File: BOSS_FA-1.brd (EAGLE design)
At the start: 50.5 x 41.9 mm, 42 parts, among them IC1 JRC4558, Q1 J201, SW1 SPST

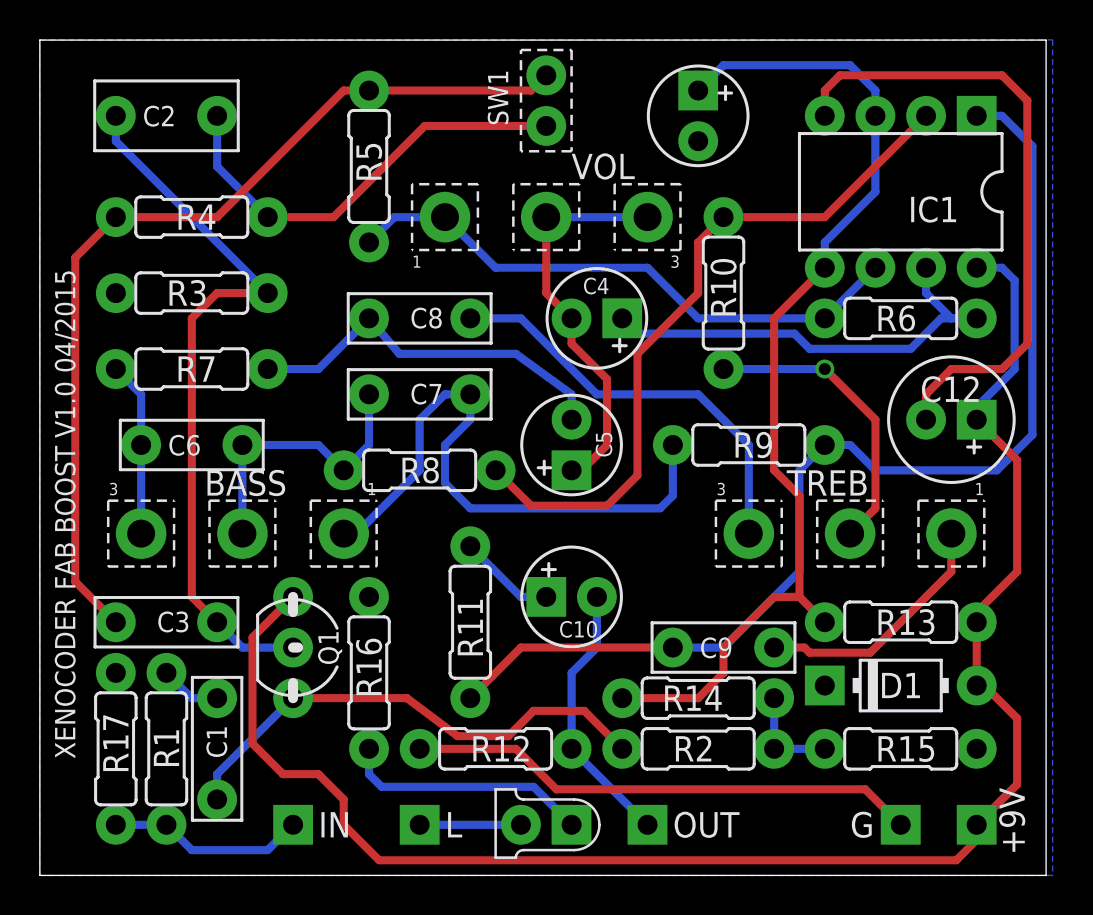
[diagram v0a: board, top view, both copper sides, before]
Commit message: Fixed Diode 1 orientation and connected power rail to LED (Version 1.1)
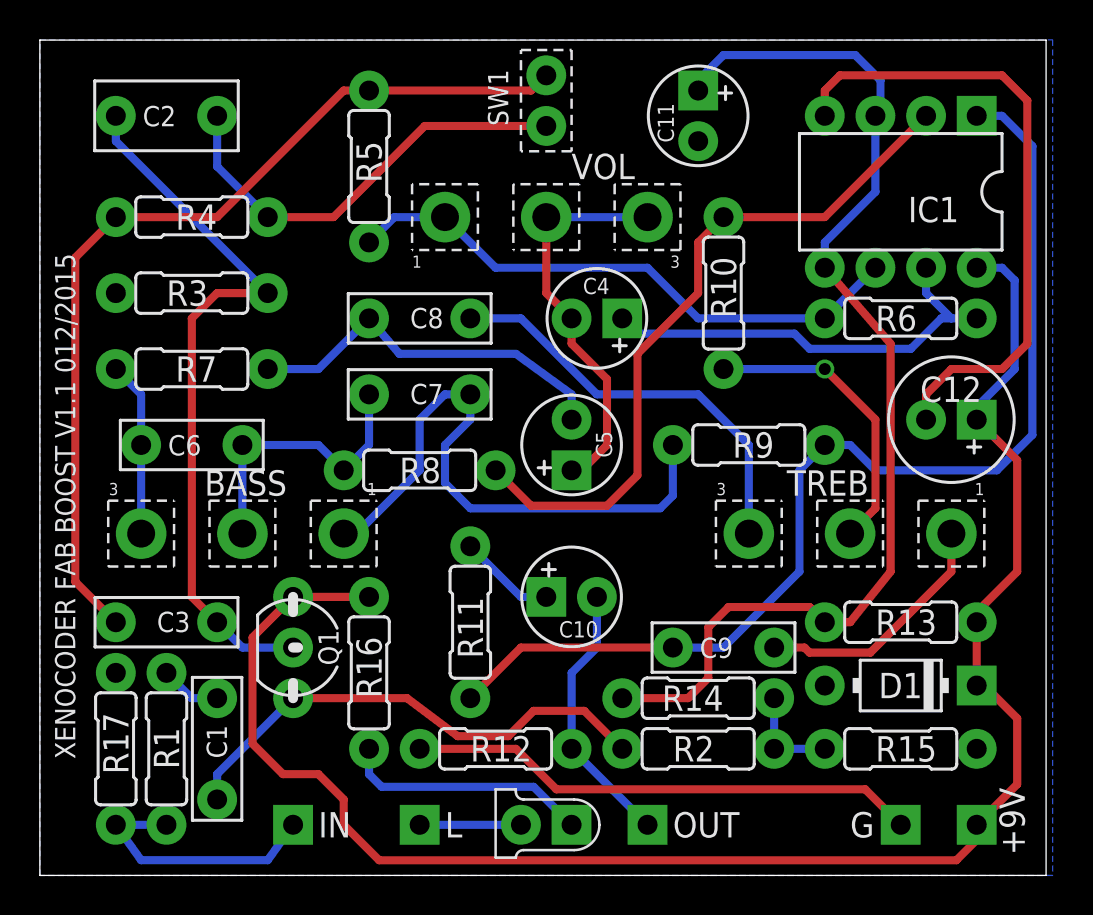
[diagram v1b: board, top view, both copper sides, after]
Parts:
- turned D1 to 180 degrees
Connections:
- net ICNET renamed A
- net LED renamed IN
- net +9V: now also D1.C; no longer D1.A
- net GND: now also D1.A; no longer D1.C
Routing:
- net A: track 51.5 -> 56.1 mm
- net +9V: track 82.7 -> 86.5 mm
- net IN: track 9.94 -> 13.3 mm
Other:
- board text added: "XENOCODER FAB BOOST V1.1 012/2015"
- board text removed: "XENOCODER FAB BOOST V1.0 04/2015"
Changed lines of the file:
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@@
 <?xml version="1.0" encoding="utf-8"?>
 <!DOCTYPE eagle SYSTEM "eagle.dtd">
-<eagle version="7.2.0">
+<eagle version="7.4.0">
 <drawing>
 <settings>
@@
 <wire x1="50.47" y1="41.9" x2="0" y2="41.9" width="0" layer="20"/>
 <wire x1="0" y1="41.9" x2="0" y2="0" width="0" layer="20"/>
-<text x="1.778" y="5.842" size="1.016" layer="25" font="vector" ratio="5" rot="R90">XENOCODER FAB BOOST V1.0 04/2015</text>
+<text x="1.778" y="5.842" size="1.016" layer="25" font="vector" ratio="5" rot="R90">XENOCODER FAB BOOST V1.1 012/2015</text>
 </plain>
 <attributes>
@@
 <attribute name="NAME" x="26.035" y="11.938" size="0.8128" layer="25" ratio="12"/>
 </element>
-<element name="C11" library="mb_caps-electro" package="050_020_1" value="10uF" x="33.02" y="38.1" smashed="yes" rot="R270"/>
+<element name="C11" library="mb_caps-electro" package="050_020_1" value="10uF" x="33.02" y="38.1" smashed="yes" rot="R270">
+<attribute name="NAME" x="30.988" y="38.735" size="0.8128" layer="25" ratio="12" rot="R270"/>
+</element>
 <element name="C12" library="mb_caps-electro" package="063_025" value="100uF" x="45.72" y="22.86" smashed="yes" rot="R180">
 <attribute name="NAME" x="47.244" y="25.019" size="1.27" layer="25" ratio="12" rot="R180"/>
@@
 <attribute name="NAME" x="13.97" y="12.319" size="1.016" layer="25" ratio="12" rot="R270"/>
 </element>
-<element name="D1" library="mb_diodes" package="DO41-3" value="1N4001" x="43.18" y="9.525" smashed="yes">
-<attribute name="NAME" x="42.0878" y="8.89" size="1.27" layer="25" ratio="12"/>
+<element name="D1" library="mb_diodes" package="DO41-3" value="1N4001" x="43.18" y="9.525" smashed="yes" rot="R180">
+<attribute name="NAME" x="44.2722" y="10.16" size="1.27" layer="25" ratio="12" rot="R180"/>
 </element>
 <element name="VOL" library="mb_pots" package="16MM_PCB_PADS" value="A1M" x="25.4" y="33.02" smashed="yes" rot="R180">
@@
 </elements>
 <signals>
-<signal name="LED">
-<contactref element="IN" pad="1"/>
-<contactref element="R17" pad="1"/>
-<contactref element="R1" pad="1"/>
-<wire x1="12.7" y1="2.54" x2="11.43" y2="1.27" width="0.4064" layer="16"/>
-<wire x1="11.43" y1="1.27" x2="7.62" y2="1.27" width="0.4064" layer="16"/>
-<wire x1="7.62" y1="1.27" x2="6.35" y2="2.54" width="0.4064" layer="16"/>
-<wire x1="3.81" y1="2.54" x2="6.35" y2="2.54" width="0.4064" layer="16"/>
-</signal>
 <signal name="GND">
 <contactref element="R17" pad="2"/>
@@
 <contactref element="R15" pad="2"/>
 <contactref element="R3" pad="1"/>
-<contactref element="D1" pad="C"/>
 <contactref element="C12" pad="-"/>
 <contactref element="R12" pad="1"/>
@@
 <wire x1="40.132" y1="40.132" x2="39.37" y2="39.37" width="0.4064" layer="1"/>
 <wire x1="39.37" y1="39.37" x2="39.37" y2="38.1" width="0.4064" layer="1"/>
+<contactref element="D1" pad="A"/>
 </signal>
 <signal name="N$1">
@@
 <wire x1="8.89" y1="8.89" x2="7.62" y2="8.89" width="0.4064" layer="16"/>
 <wire x1="7.62" y1="8.89" x2="6.35" y2="10.16" width="0.4064" layer="16"/>
-</signal>
-<signal name="ICNET">
-<contactref element="IC1" pad="3"/>
-<contactref element="IC1" pad="5"/>
-<contactref element="R14" pad="2"/>
-<contactref element="R13" pad="1"/>
-<contactref element="C11" pad="+"/>
-<wire x1="41.91" y1="38.1" x2="41.91" y2="34.29" width="0.4064" layer="16"/>
-<wire x1="41.91" y1="34.29" x2="39.37" y2="31.75" width="0.4064" layer="16"/>
-<wire x1="39.37" y1="31.75" x2="39.37" y2="30.48" width="0.4064" layer="16"/>
-<wire x1="39.37" y1="30.48" x2="36.83" y2="27.94" width="0.4064" layer="1"/>
-<wire x1="36.83" y1="27.94" x2="36.83" y2="20.32" width="0.4064" layer="1"/>
-<wire x1="36.83" y1="20.32" x2="38.1" y2="19.05" width="0.4064" layer="1"/>
-<wire x1="38.1" y1="19.05" x2="38.1" y2="13.97" width="0.4064" layer="1"/>
-<wire x1="38.1" y1="13.97" x2="39.37" y2="12.7" width="0.4064" layer="1"/>
-<wire x1="38.1" y1="13.97" x2="36.83" y2="13.97" width="0.4064" layer="1"/>
-<wire x1="36.83" y1="13.97" x2="34.29" y2="11.43" width="0.4064" layer="1"/>
-<wire x1="34.29" y1="11.43" x2="34.29" y2="10.16" width="0.4064" layer="1"/>
-<wire x1="34.29" y1="10.16" x2="33.02" y2="8.89" width="0.4064" layer="1"/>
-<wire x1="33.02" y1="8.89" x2="29.21" y2="8.89" width="0.4064" layer="1"/>
-<wire x1="33.02" y1="39.37" x2="34.29" y2="40.64" width="0.4064" layer="16"/>
-<wire x1="34.29" y1="40.64" x2="40.64" y2="40.64" width="0.4064" layer="16"/>
-<wire x1="40.64" y1="40.64" x2="41.91" y2="39.37" width="0.4064" layer="16"/>
-<wire x1="41.91" y1="39.37" x2="41.91" y2="38.1" width="0.4064" layer="16"/>
 </signal>
 <signal name="N$6">
@@
 <contactref element="R13" pad="2"/>
 <contactref element="C12" pad="+"/>
-<contactref element="D1" pad="A"/>
 <contactref element="Q1" pad="3"/>
-<contactref element="R16" pad="2"/>
 <wire x1="46.99" y1="30.48" x2="48.26" y2="30.48" width="0.4064" layer="16"/>
 <wire x1="48.26" y1="30.48" x2="48.895" y2="29.845" width="0.4064" layer="16"/>
@@
 <wire x1="48.895" y1="25.4" x2="46.99" y2="23.495" width="0.4064" layer="16"/>
 <wire x1="46.99" y1="23.495" x2="46.99" y2="22.86" width="0.4064" layer="16"/>
-<wire x1="46.99" y1="12.7" x2="46.99" y2="9.525" width="0.4064" layer="1"/>
 <wire x1="46.99" y1="2.54" x2="49.022" y2="4.572" width="0.4064" layer="1"/>
 <wire x1="49.022" y1="4.572" x2="49.022" y2="7.874" width="0.4064" layer="1"/>
 <wire x1="49.022" y1="7.874" x2="47.371" y2="9.525" width="0.4064" layer="1"/>
-<wire x1="47.371" y1="9.525" x2="46.99" y2="9.525" width="0.4064" layer="1"/>
 <wire x1="12.7" y1="13.97" x2="10.668" y2="11.938" width="0.4064" layer="1"/>
 <wire x1="10.668" y1="11.938" x2="10.668" y2="6.604" width="0.4064" layer="1"/>
@@
 <wire x1="49.022" y1="15.24" x2="49.022" y2="20.828" width="0.4064" layer="1"/>
 <wire x1="49.022" y1="20.828" x2="46.99" y2="22.86" width="0.4064" layer="1"/>
-<wire x1="12.7" y1="13.97" x2="16.51" y2="13.97" width="0" layer="19" extent="1-1"/>
+<contactref element="D1" pad="C"/>
+<contactref element="R16" pad="2"/>
+<wire x1="47.371" y1="9.525" x2="46.99" y2="9.525" width="0.4064" layer="1"/>
+<wire x1="46.99" y1="9.525" x2="46.99" y2="12.7" width="0.4064" layer="1"/>
+<wire x1="16.51" y1="13.97" x2="12.7" y2="13.97" width="0.4064" layer="1"/>
 </signal>
 <signal name="N$3">
@@
 <wire x1="35.56" y1="21.59" x2="35.56" y2="17.145" width="0.4064" layer="16"/>
 </signal>
+<signal name="IN">
+<contactref element="R1" pad="1"/>
+<contactref element="IN" pad="1"/>
+<contactref element="R17" pad="1"/>
+<wire x1="12.7" y1="2.54" x2="11.43" y2="0.762" width="0.4064" layer="16"/>
+<wire x1="11.43" y1="0.762" x2="5.08" y2="0.762" width="0.4064" layer="16"/>
+<wire x1="5.08" y1="0.762" x2="3.81" y2="2.54" width="0.4064" layer="16"/>
+<wire x1="6.35" y1="2.54" x2="3.81" y2="2.54" width="0.4064" layer="16"/>
+</signal>
+<signal name="A">
+<contactref element="C11" pad="+"/>
+<contactref element="IC1" pad="5"/>
+<contactref element="R13" pad="1"/>
+<contactref element="R14" pad="2"/>
+<contactref element="IC1" pad="3"/>
+<wire x1="33.02" y1="39.37" x2="33.02" y2="39.878" width="0.4064" layer="16"/>
+<wire x1="33.02" y1="39.878" x2="34.29" y2="41.148" width="0.4064" layer="16"/>
+<wire x1="34.29" y1="41.148" x2="40.894" y2="41.148" width="0.4064" layer="16"/>
+<wire x1="40.894" y1="41.148" x2="42.164" y2="39.878" width="0.4064" layer="16"/>
+<wire x1="42.164" y1="39.878" x2="42.164" y2="38.354" width="0.4064" layer="16"/>
+<wire x1="42.164" y1="38.354" x2="41.91" y2="38.1" width="0.4064" layer="16"/>
+<wire x1="39.37" y1="30.48" x2="39.37" y2="31.75" width="0.4064" layer="16"/>
+<wire x1="39.37" y1="31.75" x2="41.91" y2="34.29" width="0.4064" layer="16"/>
+<wire x1="41.91" y1="34.29" x2="41.91" y2="38.1" width="0.4064" layer="16"/>
+<wire x1="39.37" y1="12.7" x2="40.64" y2="12.7" width="0.4064" layer="1"/>
+<wire x1="40.64" y1="12.7" x2="42.672" y2="15.24" width="0.4064" layer="1"/>
+<wire x1="42.672" y1="15.24" x2="42.672" y2="26.67" width="0.4064" layer="1"/>
+<wire x1="42.672" y1="26.67" x2="39.37" y2="30.48" width="0.4064" layer="1"/>
+<wire x1="29.21" y1="8.89" x2="32.512" y2="8.89" width="0.4064" layer="1"/>
+<wire x1="32.512" y1="8.89" x2="33.528" y2="9.906" width="0.4064" layer="1"/>
+<wire x1="33.528" y1="9.906" x2="33.528" y2="12.446" width="0.4064" layer="1"/>
+<wire x1="33.528" y1="12.446" x2="34.544" y2="13.462" width="0.4064" layer="1"/>
+<wire x1="34.544" y1="13.462" x2="38.608" y2="13.462" width="0.4064" layer="1"/>
+<wire x1="38.608" y1="13.462" x2="39.37" y2="12.7" width="0.4064" layer="1"/>
+</signal>
 </signals>
